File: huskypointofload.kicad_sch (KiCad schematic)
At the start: 11 parts, among them J1 POWER, J2 RFSOC_POWER, J39 10MHZ, U27 ADL8124, U28 LT3093xMSE

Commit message: wip stuff
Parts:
- removed U27: ADL8124, Package_CSP:LFCSP-8_2x2mm_P0.5mm, symbol huskylib:ADL8124
- added J16: Conn_01x04_Pin, symbol Connector:Conn_01x04_Pin
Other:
- added sheet Recieve Chain (rx_chain.kicad_sch)
- moved on the sheet: U28
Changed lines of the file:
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@@
 	(symbol
 		(lib_id "Regulator_Linear:LT3093xMSE")
-		(at 132.08 138.43 0)
+		(at 91.44 189.23 0)
 		(unit 1)
 		(exclude_from_sim no)
@@
 		(fields_autoplaced yes)
 		(property "Reference" "U28"
-			(at 132.08 125.73 0)
+			(at 91.44 176.53 0)
 			(effects
 				(font
@@
 		)
 		(property "Value" "LT3093xMSE"
-			(at 132.08 128.27 0)
+			(at 91.44 179.07 0)
 			(effects
 				(font
@@
 		)
 		(property "Footprint" "Package_SO:MSOP-12-1EP_3x4.039mm_P0.65mm_EP1.651x2.845mm"
-			(at 132.08 127.635 0)
+			(at 91.44 178.435 0)
 			(effects
 				(font
@@
 		)
 		(property "Datasheet" "https://www.analog.com/media/en/technical-documentation/data-sheets/lt3093.pdf"
-			(at 132.08 135.89 0)
+			(at 91.44 186.69 0)
 			(effects
 				(font
@@
 		)
 		(property "Description" "-200mA, Adjustable, Ultralow Noise, Ultrahigh PSRR RF Negative Linear Regulator, MSOP-12"
-			(at 132.08 138.43 0)
+			(at 91.44 189.23 0)
 			(effects
 				(font
@@
 				(path "/eb9c972b-d134-41da-be97-ece3f463f7e0"
 					(reference "U28")
-					(unit 1)
-				)
-			)
-		)
-	)
-	(symbol
-		(lib_id "huskylib:ADL8124")
-		(at 147.32 102.87 0)
-		(unit 1)
-		(exclude_from_sim no)
-		(in_bom yes)
-		(on_board yes)
-		(dnp no)
-		(fields_autoplaced yes)
-		(property "Reference" "U27"
-			(at 135.89 91.948 0)
-			(do_not_autoplace yes)
-			(effects
-				(font
-					(size 1.27 1.27)
-				)
-				(justify left bottom)
-			)
-		)
-		(property "Value" "ADL8124"
-			(at 135.89 93.726 0)
-			(do_not_autoplace yes)
-			(effects
-				(font
-					(size 1.27 1.27)
-				)
-				(justify left bottom)
-			)
-		)
-		(property "Footprint" "Package_CSP:LFCSP-8_2x2mm_P0.5mm"
-			(at 147.32 102.87 0)
-			(effects
-				(font
-					(size 1.27 1.27)
-				)
-				(hide yes)
-			)
-		)
-		(property "Datasheet" "https://www.analog.com/media/en/technical-documentation/data-sheets/adl8124.pdf"
-			(at 147.32 102.87 0)
-			(effects
-				(font
-					(size 1.27 1.27)
-				)
-				(hide yes)
-			)
-		)
-		(property "Description" ""
-			(at 147.32 102.87 0)
-			(effects
-				(font
-					(size 1.27 1.27)
-				)
-				(hide yes)
-			)
-		)
-		(pin "4"
-		)
-		(pin "9"
-		)
-		(pin "4"
-		)
-		(pin "5"
-		)
-		(pin "7"
-		)
-		(pin "1"
-		)
-		(pin "3"
-		)
-		(pin "6"
-		)
-		(pin "8"
-		)
-		(pin "8"
-		)
-		(instances
-			(project ""
-				(path "/eb9c972b-d134-41da-be97-ece3f463f7e0"
-					(reference "U27")
 					(unit 1)
 				)
@@
 	)
 	(symbol
+		(lib_id "Connector:Conn_01x04_Pin")
+		(at 148.59 187.96 0)
+		(unit 1)
+		(exclude_from_sim no)
+		(in_bom yes)
+		(on_board yes)
+		(dnp no)
+		(fields_autoplaced yes)
+		(property "Reference" "J16"
+			(at 149.225 180.34 0)
+			(effects
+				(font
+					(size 1.27 1.27)
+				)
+				(hide yes)
+			)
+		)
+		(property "Value" "Conn_01x04_Pin"
+			(at 149.225 182.88 0)
+			(effects
+				(font
+					(size 1.27 1.27)
+				)
+			)
+		)
+		(property "Footprint" ""
+			(at 148.59 187.96 0)
+			(effects
+				(font
+					(size 1.27 1.27)
+				)
+				(hide yes)
+			)
+		)
+		(property "Datasheet" "~"
+			(at 148.59 187.96 0)
+			(effects
+				(font
+					(size 1.27 1.27)
+				)
+				(hide yes)
+			)
+		)
+		(property "Description" "Generic connector, single row, 01x04, script generated"
+			(at 148.59 187.96 0)
+			(effects
+				(font
+					(size 1.27 1.27)
+				)
+				(hide yes)
+			)
+		)
+		(pin "3"
+		)
+		(pin "4"
+		)
+		(pin "2"
+		)
+		(pin "1"
+		)
+		(instances
+			(project ""
+				(path "/eb9c972b-d134-41da-be97-ece3f463f7e0"
+					(reference "J16")
+					(unit 1)
+				)
+			)
+		)
+	)
+	(symbol
 		(lib_id "Connector:Screw_Terminal_01x02")
 		(at 63.5 43.18 270)
@@
 	)
 	(sheet
-		(at 213.36 83.82)
+		(at 218.44 106.68)
 		(size 16.51 10.16)
 		(exclude_from_sim no)
@@
 		)
 		(property "Sheetname" "Bias Generator"
-			(at 213.36 83.1084 0)
+			(at 218.44 105.9684 0)
 			(effects
 				(font
@@
 		)
 		(property "Sheetfile" "bias_gen.kicad_sch"
-			(at 213.36 94.5646 0)
+			(at 218.44 117.4246 0)
 			(effects
 				(font
@@
 				)
 			)
+		)
+	)
+	(sheet
+		(at 255.27 106.68)
+		(size 52.07 15.24)
+		(exclude_from_sim no)
+		(in_bom yes)
+		(on_board yes)
+		(dnp no)
+		(fields_autoplaced yes)
+		(stroke
+			(width 0.1524)
+			(type solid)
+		)
+		(fill
+			(color 0 0 0 0.0000)
+		)
+		(property "Sheetname" "Recieve Chain"
+			(at 255.27 105.9684 0)
+			(effects
+				(font
+					(size 1.27 1.27)
+				)
+				(justify left bottom)
+			)
+		)
+		(property "Sheetfile" "rx_chain.kicad_sch"
+			(at 255.27 122.5046 0)
+			(effects
+				(font
+					(size 1.27 1.27)
+				)
+				(justify left top)
+			)
+		)
+		(instances
+			(project "huskypointofload"
+				(path "/eb9c972b-d134-41da-be97-ece3f463f7e0"
+					(page "23")
+				)
+			)

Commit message: For Darrel
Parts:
- removed D1: DFLS1150, Diode_SMD:D_PowerDI-123, symbol Device:D_Schottky_Small
- removed J1: POWER, TerminalBlock_WAGO:TerminalBlock_WAGO_2601-1105_1x05_P3.50mm_Horizontal, symbol Connector:Screw_Terminal_01x05
- removed J16: Conn_01x04_Pin, symbol Connector:Conn_01x04_Pin
- removed J2: RFSOC_POWER, TerminalBlock_WAGO:TerminalBlock_WAGO_2601-1102_1x02_P3.50mm_Horizontal, symbol Connector:Screw_Terminal_01x02
- removed J39: 10MHZ, symbol Connector:Conn_Coaxial_Small
- removed U28: LT3093xMSE, Package_SO:MSOP-12-1EP_3x4.039mm_P0.65mm_EP1.651x2.845mm, symbol Regulator_Linear:LT3093xMSE
- added J1: Barrel_Jack, symbol Connector:Barrel_Jack
- added J2: FROM_FRIDGE, symbol Connector:Conn_Coaxial_Small
- added J3: TO_FRIDGE, symbol Connector:Conn_Coaxial_Small
- added J4: ADC_C, symbol Connector:Conn_Coaxial_Small
- added J5: ADC_D, symbol Connector:Conn_Coaxial_Small
- added J6: DAC_A, symbol Connector:Conn_Coaxial_Small
- added J7: DAC_B, symbol Connector:Conn_Coaxial_Small
- renumbered D2 to D1, D3 to D2, D4 to D3
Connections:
- net +VDC: now also J1.1
- net GND: now also J1.2, J2.2 (Ext), J3.2 (Ext), J4.2 (Ext), J5.2 (Ext), J6.2 (Ext), J7.2 (Ext)
- net TX Mixer/I: now also J6.1 (In)
- net TX Mixer/Q: now also J7.1 (In)
- new net RX Mixer/I: J4.1 (In)
- new net RX Mixer/Q: J5.1 (In)
- new net Recieve Chain/RFIN: J2.1 (In)
- no-connect marks 2 -> 3
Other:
- removed sheet 10MHz Dist
- removed sheet IBC
- added sheet Clocking (clocking.kicad_sch)
- added sheet RX Mixer (hmc525.kicad_sch)
- sheet Bias Generator ports: added A0, A1, BIASA, BIASB, BIASC, BIASD, SCL, SDA, ~{LDAC}; removed none
- sheet MCU ports: added CIPO, COPI; removed BUCKIN_SENSE, BUCKOUT_SENSE, EN_IBC, HS_SWITCH, LS_SWITCH, MISO, MOSI, SOC_ISENSE
- sheet RF Supplies ports: added EN_RF6TX, PG_RF6TX, SYNC_RF6TX; removed DIST_EN, DIST_PG, SOC_ISENSE
- sheet Recieve Chain ports: added CIPO, COPI, EN_{AMP0}, EN_{AMP1}, EN_{AMP2}, RFIN, RFOUT, SCK, VTEMP, ~{CS_{AMP1}}, ~{CS_{AMP2}}; removed none
- note added: "TODO: Equalization (Marki positive slope MMIC) Maybe directional coupler to other ADCA/B"
- note added: "TODO: Update Power Tree TODO: Add Clock Tree"
- note added: "Transmit Chain TODO: Equalizer, filter, and PE43705 possibly one amplifier"
- note removed: "10A FUSE 250mV/A ISENSE"
- note removed: "10V"
- note removed: "12V"
- note removed: "48V"
- note removed: "48V to 12V DCDC for RFSoC and RF Low Noise PSUs Designed for 13A at 12V, RFSoC will take 10A. Passives rated for an EPC23102 for a 25A upgrade"
- note removed: "EPC23104 IBC 48V->12V15A"
- note removed: "LT3045 12V->10V0.8A"
- note removed: "RATED TO 63V MAX"
- note removed: "RFSoC"
- moved on the sheet: D1, D2, D3, R1, R2

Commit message: wip
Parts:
- added R143: 453k, Resistor_SMD:R_0402_1005Metric, symbol Device:R_Small
- added R144: 60k, Resistor_SMD:R_0402_1005Metric, symbol Device:R_Small
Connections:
- net GND: now also R144.2
- net Transmit Chain/RFOUT: now reaches J3.1 (In)
- new net Linear POL LMK VCO/PGFB+: R143.1
- new net Linear POL LMK VCO/PGFB-: R143.2
- new net Linear POL LMK VCO/SET: R144.1
- no-connect marks 3 -> 4
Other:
- removed sheet Bias Generator
- added sheet Linear POL LMK VCO (linear.kicad_sch)
- added sheet Transmit Chain (tx_chain.kicad_sch)
- note removed: "TODO: Equalization (Marki positive slope MMIC) Maybe directional coupler to other ADCA/B"
- note removed: "Transmit Chain TODO: Equalizer, filter, and PE43705 possibly one amplifier"

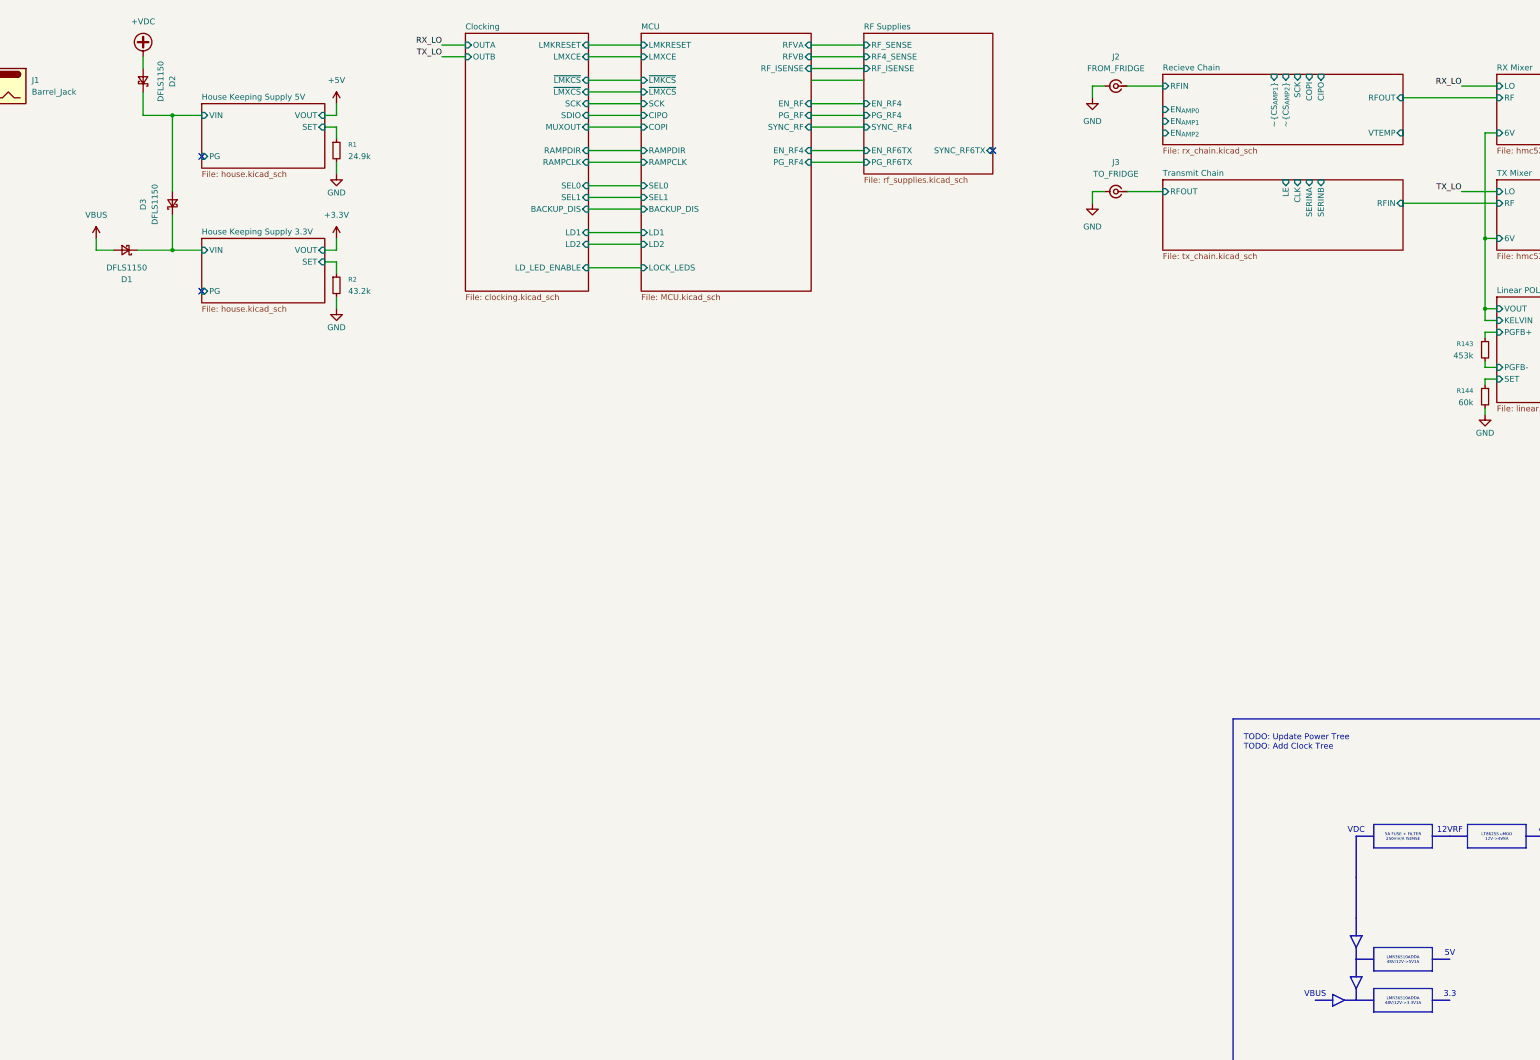
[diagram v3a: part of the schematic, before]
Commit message: Rework RF Supplies
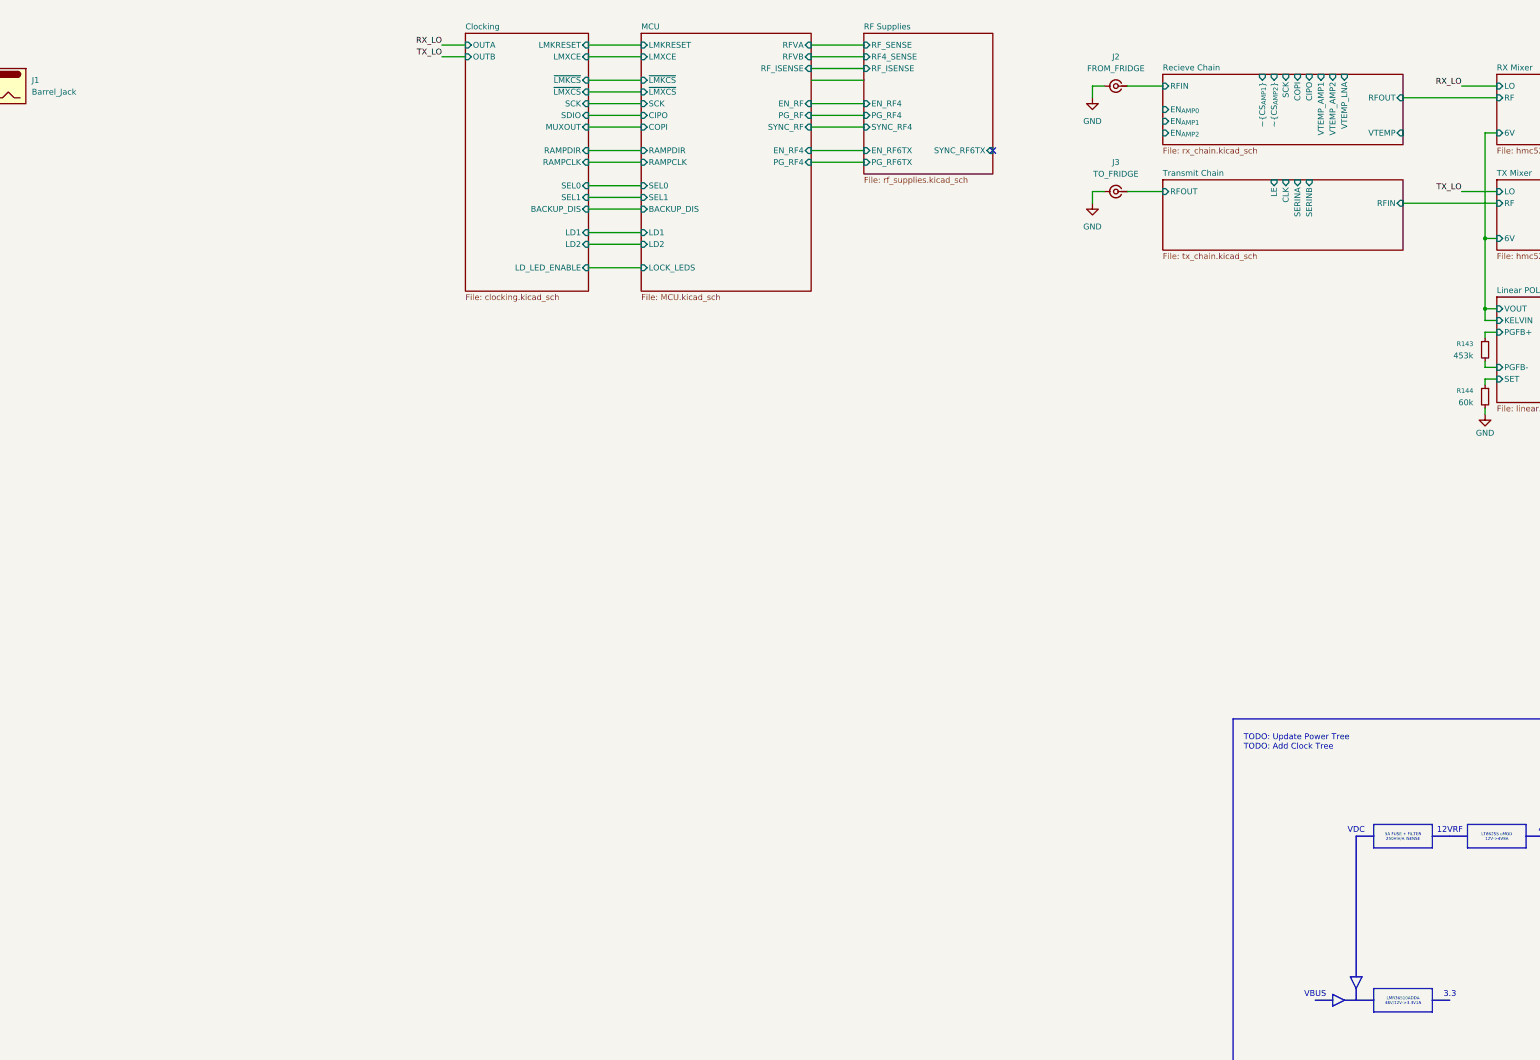
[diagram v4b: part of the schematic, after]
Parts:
- removed D1, D2, D3: DFLS1150, Diode_SMD:D_PowerDI-123, symbol Device:D_Schottky_Small
- removed R1: 24.9k, Resistor_SMD:R_0402_1005Metric, symbol Device:R_Small
- removed R2: 43.2k, Resistor_SMD:R_0402_1005Metric, symbol Device:R_Small
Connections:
- no-connect marks 4 -> 2
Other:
- removed sheet House Keeping Supply 3.3V
- removed sheet House Keeping Supply 5V
- sheet Recieve Chain ports: added VTEMP_AMP1, VTEMP_AMP2, VTEMP_LNA; removed none
- note removed: "5V"
- note removed: "LMR36510ADDA 48V/12V->5V1A"

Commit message: Add Clock sources and monitor output
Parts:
- added J12: SYNCOUT, symbol Connector:Conn_Coaxial_Small
- added J13: REFOUT, symbol Connector:Conn_Coaxial_Small
- added J14: PPSOUT, symbol Connector:Conn_Coaxial_Small
- added J2: PMOD, symbol Connector_Generic:Conn_02x06_Counter_Clockwise
- added J5: PPSIN, symbol Connector:Conn_Coaxial_Small
- added J8: ADC_A, symbol Connector:Conn_Coaxial_Small
- added J9: ADC_B, symbol Connector:Conn_Coaxial_Small
- J1: value Barrel_Jack -> POWER_IN
- renumbered J4 to J10, J5 to J11, J2 to J4, R143 to R1, R144 to R2
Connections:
- net GND: now also J2.5 (Pin_5), J2.8 (Pin_8), J8.2 (Ext), J9.2 (Ext)
- new net +1V8: J2.6 (Pin_6), J2.7 (Pin_7)
- new net Monitor Path/HP: J8.1 (In)
- new net Monitor Path/LP: J9.1 (In)
- new net PPSOUT_{n}: J14.2 (Ext), J5.2 (Ext)
- new net PPSOUT_{p}: J14.1 (In), J5.1 (In)
- new net REFOUT_{n}: J13.2 (Ext)
- new net REFOUT_{p}: J13.1 (In)
- new net RF_CIPO: J2.11 (Pin_11)
- new net RF_COPI: J2.10 (Pin_10)
- new net RF_RAMPCLK: J2.4 (Pin_4)
- new net RF_RAMPDIR: J2.3 (Pin_3)
- new net RF_SCK: J2.9 (Pin_9)
- new net SYNCOUT_{n}: J12.2 (Ext)
- new net SYNCOUT_{p}: J12.1 (In)
- new net ~{RF_CS0}: J2.2 (Pin_2)
- new net ~{RF_CS1}: J2.1 (Pin_1)
- new net ~{RF_CS2}: J2.12 (Pin_12)
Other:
- added sheet Monitor Path (monitor.kicad_sch)
- sheet Clocking ports: added PPSOUT_{n}, PPSOUT_{p}, REFOUT_{n}, REFOUT_{p}, SYNCOUT_{n}, SYNCOUT_{p}; removed none
- sheet Recieve Chain ports: added MONOUT; removed VTEMP
- note added: "ADC A"
- note added: "ADC B"
- note added: "ADC C"
- note added: "ADC D"
- note added: "DAC A"
- note added: "DAC B"
- note added: "IFBOARD"
- note added: "PPS"
- note added: "REF"
- note added: "RFSOC 4X2"
- note added: "SYNC"
- moved on the sheet: J1, J10, J11, J3, J4, J6, J7, R1, R2

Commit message: It's finished (well the draft)
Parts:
- added R? (x3): 100, symbol Device:R_Small
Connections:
- net ~{RF_CS2} is gone; now on net RF_CIPO: J2.12 (Pin_12)
- net Clocking/RAMPCLK: now also R?.2
- net Clocking/RAMPDIR: now also R?.1
- net GND: now also J2.4 (Pin_4); no longer J2.5 (Pin_5)
- net RF_CIPO: no longer J2.11 (Pin_11)
- net RF_COPI: now also J2.11 (Pin_11); no longer J2.10 (Pin_10)
- net RF_RAMPCLK: now also J2.2 (Pin_2), R?.1; no longer J2.4 (Pin_4)
- net RF_RAMPDIR: now also J2.1 (Pin_1), R?.2; no longer J2.3 (Pin_3)
- net RF_SCK: now also J2.10 (Pin_10); no longer J2.9 (Pin_9)
- net ~{RF_CS0}: now also J2.9 (Pin_9); no longer J2.2 (Pin_2)
- net ~{RF_CS1}: now also J2.3 (Pin_3); no longer J2.1 (Pin_1)
- new net MCU/RF_CLKIN: R?.2
- new net RF_CLKOUT: J2.5 (Pin_5), R?.1
- no-connect marks 2 -> 1
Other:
- sheet MCU ports: added EN_RF4RX, EN_RF7, EN_{AMP0}, EN_{AMP1}, EN_{AMP2}, PG_RF4RX, PG_RF7, RF12_ISENSE, RF12_SENSE, RF4_SENSE, RF7_SENSE, RF_CIPO, RF_CLKIN, RF_COPI, RF_SCK, SYNC_RF4, SYNC_RF4RX, SYNC_RF7, TX_CLK, TX_LE, TX_SEROUTA, TX_SEROUTB, VTEMP0, VTEMP1, VTEMP2, ~{RF_AMP1CS}, ~{RF_AMP2CS}, ~{RF_CS0}, ~{RF_CS1}; removed EN_RF, PG_RF, RFVA, RFVB, RF_ISENSE, SYNC_RF
- sheet RF Supplies ports: added EN_RF7, PG_RF7, RF12_ISENSE, RF12_SENSE, RF7_SENSE, SYNC_RF7; removed EN_RF6TX, PG_RF6TX, RF_ISENSE, RF_SENSE, SYNC_RF6TX
- sheet Recieve Chain ports: added EN_RF4RX, PG_RF4RX, SYNC_RF4RX, VTEMP_AMP0; removed VTEMP_LNA
- note added: "Pins here can be reorderd as needed to ease routing"
- moved on the sheet: J1, J12, J13, J14, J2, J3, J4, J5, J6, J7, J8, J9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

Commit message: Round 1 review comments
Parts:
- added J?: PARAMP_DRIVE, symbol Connector:Conn_Coaxial_Small
- R4: renamed from R1; value 453k -> 680k
- R5: renamed from R2; value 60k -> 50k
- gave numbers to parts that had none: 3
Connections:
- net Linear POL LMK VCO/PGFB+ is gone; now on net VCC_LODRIVE: R4.1
- net GND: now also J?.2 (Ext)
- net +1V8 renamed V_{PMOD}
- net Linear POL LMK VCO/PGFB- renamed Linear POL LMK VCO/PGFB
- new net Clocking/OUTPARAMP: J?.1 (In)
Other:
- sheet Clocking ports: added OUTPARAMP, ~{LMX_{LO}CS}; removed none
- sheet Linear POL LMK VCO ports: added PGFB; removed PGFB+, PGFB-
- note added: "Populate both output caps"
- moved on the sheet: J1, J10, J11, J12, J13, J14, J2, J3, J4, J5, J6, J7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
